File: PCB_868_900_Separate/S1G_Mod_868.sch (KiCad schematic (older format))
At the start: 53 parts, among them J1 S2B-PH-K-S(LF)(SN), Q1 DMG2307L-7, SW1 CUS-12TB, T1 1909763-1, T2 1909763-1, U1 AP7361-33FGE-7, U2 ADF7023BCPZ, X1 ABS07-32.768KHZ-9-T, X2 ABM11-140-26.000MHZ-T3

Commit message: Change and Progress
connecotrs change to SMA, implemented combined PA/LNA match, currently
working on that version as primary. PCB components are placed and board
size is almost set.
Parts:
- removed T1, T2: 1909763-1, PCB_Footprints:1909763-1, symbol 1909763-1
- added T1, T2: 0732511150, PCB_Footprints:0732511150, symbol 0732511150
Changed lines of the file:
@@
 encoding utf-8
 Sheet 1 2
-Title ""
-Date ""
-Rev ""
-Comp ""
-Comment1 ""
+Title "S1G 915MHZ RF RX/TX Module Separate PA/LNA Match"
+Date "2016-11-07"
+Rev "0.1a"
+Comp "GhostPCB"
+Comment1 "Engineered and Drawn By: Adam Vadala-Roth"
 Comment2 ""
 Comment3 ""
@@
 $EndComp
 $Comp
-L 1909763-1 T2
-U 1 1 5817C82C
-P 725 4600
-F 0 "T2" H 700 4825 60  0000 L CNN
-F 1 "1909763-1" H 275 4725 60  0000 L CNN
-F 2 "PCB_Footprints:1909763-1" H 775 4450 60  0001 C CNN
-F 3 "https://media.digikey.com/pdf/PCNs/TE%20Connectivity/E-15-016061(2).pdf" H 425 4775 60  0001 C CNN
-F 4 "0.24000 @ 5000" H 525 4875 60  0001 C CNN "Cost"
-F 5 "8 Sept 2016" H 625 4975 60  0001 C CNN "Date Created"
-F 6 "8 Sept 2016" H 725 5075 60  0001 C CNN "Date Modified"
-F 7 "Adam Vadala-Roth" H 825 5175 60  0001 C CNN "Designer"
-F 8 "1.25mm" H 925 5275 60  0001 C CNN "Height"
-F 9 "Yes" H 1025 5375 60  0001 C CNN "RHoS?"
-F 10 "TE Connectivity AMP Connectors" H 1125 5475 60  0001 C CNN "MFR"
-F 11 "1909763-1" H 1225 5575 60  0001 C CNN "MFR#"
-F 12 "SMT/SMD" H 1325 5675 60  0001 C CNN "Mounting"
-F 13 "2" H 1425 5775 60  0001 C CNN "Pin Count#"
-F 14 "Active" H 1525 5875 60  0001 C CNN "Status"
-F 15 "N/A" H 1625 5975 60  0001 C CNN "Tolerance"
-F 16 "Coaxial RF Connector" H 1725 6075 60  0001 C CNN "Type"
-F 17 "N/A" H 1825 6175 60  0001 C CNN "Voltage"
-F 18 "N/A" H 1925 6275 60  0001 C CNN "Wattage"
-F 19 "50 ohm" H 2025 6375 60  0001 C CNN "Component-Value"
-F 20 "Ultra Miniature Coaxial Connector Jack, Male Pin 50 Ohm Surface Mount Solder" H 2125 6475 60  0001 C CNN "Description"
-	1    725  4600
-	-1   0    0    -1
-$EndComp
-$Comp
 L 0402CS-12NXJL L1
 U 1 1 5817F234
@@
 $EndComp
 $Comp
-L 1909763-1 T1
-U 1 1 5819761C
-P 700 3375
-F 0 "T1" H 675 3600 60  0000 L CNN
-F 1 "1909763-1" H 250 3500 60  0000 L CNN
-F 2 "PCB_Footprints:1909763-1" H 750 3225 60  0001 C CNN
-F 3 "https://media.digikey.com/pdf/PCNs/TE%20Connectivity/E-15-016061(2).pdf" H 400 3550 60  0001 C CNN
-F 4 "0.24000 @ 5000" H 500 3650 60  0001 C CNN "Cost"
-F 5 "8 Sept 2016" H 600 3750 60  0001 C CNN "Date Created"
-F 6 "8 Sept 2016" H 700 3850 60  0001 C CNN "Date Modified"
-F 7 "Adam Vadala-Roth" H 800 3950 60  0001 C CNN "Designer"
-F 8 "1.25mm" H 900 4050 60  0001 C CNN "Height"
-F 9 "Yes" H 1000 4150 60  0001 C CNN "RHoS?"
-F 10 "TE Connectivity AMP Connectors" H 1100 4250 60  0001 C CNN "MFR"
-F 11 "1909763-1" H 1200 4350 60  0001 C CNN "MFR#"
-F 12 "SMT/SMD" H 1300 4450 60  0001 C CNN "Mounting"
-F 13 "2" H 1400 4550 60  0001 C CNN "Pin Count#"
-F 14 "Active" H 1500 4650 60  0001 C CNN "Status"
-F 15 "N/A" H 1600 4750 60  0001 C CNN "Tolerance"
-F 16 "Coaxial RF Connector" H 1700 4850 60  0001 C CNN "Type"
-F 17 "N/A" H 1800 4950 60  0001 C CNN "Voltage"
-F 18 "N/A" H 1900 5050 60  0001 C CNN "Wattage"
-F 19 "50 ohm" H 2000 5150 60  0001 C CNN "Component-Value"
-F 20 "Ultra Miniature Coaxial Connector Jack, Male Pin 50 Ohm Surface Mount Solder" H 2100 5250 60  0001 C CNN "Description"
-	1    700  3375
-	-1   0    0    -1
-$EndComp
-$Comp
 L GND #PWR1
 U 1 1 581979F7
@@
 L S2B-PH-K-S(LF)(SN) J1
 U 1 1 58229495
-P 1050 6125
-F 0 "J1" H 1000 6400 60  0000 C CNN
-F 1 "S2B-PH-K-S(LF)(SN)" H 1450 6325 60  0000 C CNN
-F 2 "PCB_Footprints:S2B-PH-K-S(LF)(SN)" H 900 6200 60  0001 C CNN
-F 3 "http://www.jst-mfg.com/product/pdf/eng/ePH.pdf" H 775 6500 60  0001 C CNN
-F 4 "0.06152 @ 5000" H 875 6600 60  0001 C CNN "Cost"
-F 5 "9 Sept 2016" H 975 6700 60  0001 C CNN "Date Created "
-F 6 "9 Sept 2016" H 1075 6800 60  0001 C CNN "Date Modified"
-F 7 "Adam Vadala-Roth" H 1175 6900 60  0001 C CNN "Designer "
-F 8 "5.5mm" H 1275 7000 60  0001 C CNN "Height"
-F 9 "Yes" H 1375 7100 60  0001 C CNN "RHoS?"
-F 10 "JST Sales America Inc" H 1475 7200 60  0001 C CNN "MFR"
-F 11 "S2B-PH-K-S(LF)(SN)" H 1575 7300 60  0001 C CNN "MFR#"
-F 12 "Through Hole" H 1675 7400 60  0001 C CNN "Mounting"
-F 13 "2" H 1775 7500 60  0001 C CNN "Pin Count#"
-F 14 "Active" H 1875 7600 60  0001 C CNN "Status"
-F 15 "N/A" H 1975 7700 60  0001 C CNN "Tolerance"
-F 16 "Through Hole right angle connector." H 2075 7800 60  0001 C CNN "Type"
-F 17 "N/A" H 2175 7900 60  0001 C CNN "Voltage"
-F 18 "N/A" H 2275 8000 60  0001 C CNN "Wattage"
-F 19 "N/A" H 2375 8100 60  0001 C CNN "Component-Value"
-F 20 "2 Positions Header, Shrouded Connector 0.079\" (2.00mm) Through Hole, Right Angle Tin" H 2475 8200 60  0001 C CNN "Description"
-	1    1050 6125
-	1    0    0    -1
+P 1050 6050
+F 0 "J1" H 1000 6325 60  0000 C CNN
+F 1 "S2B-PH-K-S(LF)(SN)" H 1450 6250 60  0000 C CNN
+F 2 "PCB_Footprints:S2B-PH-K-S(LF)(SN)" H 900 6125 60  0001 C CNN
+F 3 "http://www.jst-mfg.com/product/pdf/eng/ePH.pdf" H 775 6425 60  0001 C CNN
+F 4 "0.06152 @ 5000" H 875 6525 60  0001 C CNN "Cost"
+F 5 "9 Sept 2016" H 975 6625 60  0001 C CNN "Date Created "
+F 6 "9 Sept 2016" H 1075 6725 60  0001 C CNN "Date Modified"
+F 7 "Adam Vadala-Roth" H 1175 6825 60  0001 C CNN "Designer "
+F 8 "5.5mm" H 1275 6925 60  0001 C CNN "Height"
+F 9 "Yes" H 1375 7025 60  0001 C CNN "RHoS?"
+F 10 "JST Sales America Inc" H 1475 7125 60  0001 C CNN "MFR"
+F 11 "S2B-PH-K-S(LF)(SN)" H 1575 7225 60  0001 C CNN "MFR#"
+F 12 "Through Hole" H 1675 7325 60  0001 C CNN "Mounting"
+F 13 "2" H 1775 7425 60  0001 C CNN "Pin Count#"
+F 14 "Active" H 1875 7525 60  0001 C CNN "Status"
+F 15 "N/A" H 1975 7625 60  0001 C CNN "Tolerance"
+F 16 "Through Hole right angle connector." H 2075 7725 60  0001 C CNN "Type"
+F 17 "N/A" H 2175 7825 60  0001 C CNN "Voltage"
+F 18 "N/A" H 2275 7925 60  0001 C CNN "Wattage"
+F 19 "N/A" H 2375 8025 60  0001 C CNN "Component-Value"
+F 20 "2 Positions Header, Shrouded Connector 0.079\" (2.00mm) Through Hole, Right Angle Tin" H 2475 8125 60  0001 C CNN "Description"
+	1    1050 6050
+	1    0    0    1
 $EndComp
 $Comp
@@
 Wire Wire Line
 	9375 3800 8950 3800
+$Comp
+L 0732511150 T1
+U 1 1 5828483C
+P 700 3375
+F 0 "T1" H 700 3575 60  0000 L CNN
+F 1 "0732511150" H 225 3500 60  0000 L CNN
+F 2 "PCB_Footprints:0732511150" H 750 3225 60  0001 C CNN
+F 3 "http://www.molex.com/pdm_docs/sd/732511150_sd.pdf" H 400 3550 60  0001 C CNN
+F 4 "1.929370 @ 1000" H 500 3650 60  0001 C CNN "Cost"
+F 5 "7 Nov 2016" H 600 3750 60  0001 C CNN "Date Created"
+F 6 "7 Nov 2016" H 700 3850 60  0001 C CNN "Date Modified"
+F 7 "Adam Vadala-Roth" H 800 3950 60  0001 C CNN "Designer"
+F 8 "1.25mm" H 900 4050 60  0001 C CNN "Height"
+F 9 "Yes" H 1000 4150 60  0001 C CNN "RHoS?"
+F 10 "Molex, LLC" H 1100 4250 60  0001 C CNN "MFR"
+F 11 "0732511150" H 1200 4350 60  0001 C CNN "MFR#"
+F 12 "SMT/SMD" H 1300 4450 60  0001 C CNN "Mounting"
+F 13 "2" H 1400 4550 60  0001 C CNN "Pin Count#"
+F 14 "Active" H 1500 4650 60  0001 C CNN "Status"
+F 15 "N/A" H 1600 4750 60  0001 C CNN "Tolerance"
+F 16 "SMA Coaxial RF Connector" H 1700 4850 60  0001 C CNN "Type"
+F 17 "N/A" H 1800 4950 60  0001 C CNN "Voltage"
+F 18 "N/A" H 1900 5050 60  0001 C CNN "Wattage"
+F 19 "50 ohm" H 2000 5150 60  0001 C CNN "Component-Value"
+F 20 "SMA Connector Receptacle, Female Socket 50 Ohm Board Edge, End Launch Solder" H 2100 5250 60  0001 C CNN "Description"
+	1    700  3375
+	-1   0    0    -1
+$EndComp
+$Comp
+L 0732511150 T2
+U 1 1 5828637F
+P 725 4600
+F 0 "T2" H 725 4800 60  0000 L CNN
+F 1 "0732511150" H 250 4725 60  0000 L CNN
+F 2 "PCB_Footprints:0732511150" H 775 4450 60  0001 C CNN
+F 3 "http://www.molex.com/pdm_docs/sd/732511150_sd.pdf" H 425 4775 60  0001 C CNN
+F 4 "1.929370 @ 1000" H 525 4875 60  0001 C CNN "Cost"
+F 5 "7 Nov 2016" H 625 4975 60  0001 C CNN "Date Created"
+F 6 "7 Nov 2016" H 725 5075 60  0001 C CNN "Date Modified"
+F 7 "Adam Vadala-Roth" H 825 5175 60  0001 C CNN "Designer"
+F 8 "1.25mm" H 925 5275 60  0001 C CNN "Height"
+F 9 "Yes" H 1025 5375 60  0001 C CNN "RHoS?"
+F 10 "Molex, LLC" H 1125 5475 60  0001 C CNN "MFR"
+F 11 "0732511150" H 1225 5575 60  0001 C CNN "MFR#"
+F 12 "SMT/SMD" H 1325 5675 60  0001 C CNN "Mounting"
+F 13 "2" H 1425 5775 60  0001 C CNN "Pin Count#"
+F 14 "Active" H 1525 5875 60  0001 C CNN "Status"
+F 15 "N/A" H 1625 5975 60  0001 C CNN "Tolerance"
+F 16 "SMA Coaxial RF Connector" H 1725 6075 60  0001 C CNN "Type"
+F 17 "N/A" H 1825 6175 60  0001 C CNN "Voltage"
+F 18 "N/A" H 1925 6275 60  0001 C CNN "Wattage"
+F 19 "50 ohm" H 2025 6375 60  0001 C CNN "Component-Value"
+F 20 "SMA Connector Receptacle, Female Socket 50 Ohm Board Edge, End Launch Solder" H 2125 6475 60  0001 C CNN "Description"
+	1    725  4600
+	-1   0    0    -1
+$EndComp
 $EndSCHEMATC

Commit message: License added and dedicated PA/LNA Match
Working on the separate PA/LNA match version. also added cern license
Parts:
- removed J1: S2B-PH-K-S(LF)(SN), PCB_Footprints:S2B-PH-K-S(LF)(SN), symbol S2B-PH-K-S(LF)(SN)
- added SH1: 36103205, PCB_Footprints:36103205, symbol 36103205
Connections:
- wire segments 89 -> 90
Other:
- note added: "S1G-RF 915MHZ Sub 1GHZ RF Radio Separate PA & LNA Match"
- note removed: "S1G-Mod 915MHZ Sub 1GHZ RF RX/TX Module"
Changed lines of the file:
@@
 $EndComp
 $Comp
-L GND #PWR4
+L GND #PWR3
 U 1 1 58174222
 P 2000 5050
-F 0 "#PWR4" H 2000 4800 50  0001 C CNN
+F 0 "#PWR3" H 2000 4800 50  0001 C CNN
 F 1 "GND" H 2005 4877 50  0000 C CNN
 F 2 "" H 2000 5050 50  0000 C CNN
@@
 $EndComp
 $Comp
-L GND #PWR6
+L GND #PWR5
 U 1 1 581744A7
 P 2800 5050
-F 0 "#PWR6" H 2800 4800 50  0001 C CNN
+F 0 "#PWR5" H 2800 4800 50  0001 C CNN
 F 1 "GND" H 2805 4877 50  0000 C CNN
 F 2 "" H 2800 5050 50  0000 C CNN
@@
 $EndComp
 $Comp
-L GND #PWR11
+L GND #PWR10
 U 1 1 5816BC64
 P 4000 6500
-F 0 "#PWR11" H 4000 6250 50  0001 C CNN
+F 0 "#PWR10" H 4000 6250 50  0001 C CNN
 F 1 "GND" H 4005 6327 50  0000 C CNN
 F 2 "" H 4000 6500 50  0000 C CNN
@@
 $EndComp
 $Comp
-L GND #PWR9
+L GND #PWR8
 U 1 1 5817CEBD
 P 3650 2200
-F 0 "#PWR9" H 3650 1950 50  0001 C CNN
+F 0 "#PWR8" H 3650 1950 50  0001 C CNN
 F 1 "GND" H 3655 2027 50  0000 C CNN
 F 2 "" H 3650 2200 50  0000 C CNN
@@
 $EndComp
 $Comp
-L +3.3V #PWR7
+L +3.3V #PWR6
 U 1 1 5817CF98
 P 3150 1750
-F 0 "#PWR7" H 3150 1600 50  0001 C CNN
+F 0 "#PWR6" H 3150 1600 50  0001 C CNN
 F 1 "+3.3V" H 3165 1923 50  0000 C CNN
 F 2 "" H 3150 1750 50  0000 C CNN
@@
 $EndComp
 $Comp
-L GND #PWR8
+L GND #PWR7
 U 1 1 5818E84F
 P 3600 5050
-F 0 "#PWR8" H 3600 4800 50  0001 C CNN
+F 0 "#PWR7" H 3600 4800 50  0001 C CNN
 F 1 "GND" H 3605 4877 50  0000 C CNN
 F 2 "" H 3600 5050 50  0000 C CNN
@@
 $EndComp
 $Comp
-L GND #PWR10
+L GND #PWR9
 U 1 1 58195E9E
 P 3675 4100
-F 0 "#PWR10" H 3675 3850 50  0001 C CNN
+F 0 "#PWR9" H 3675 3850 50  0001 C CNN
 F 1 "GND" H 3680 3927 50  0000 C CNN
 F 2 "" H 3675 4100 50  0000 C CNN
@@
 $EndComp
 $Comp
-L GND #PWR5
+L GND #PWR4
 U 1 1 58196935
 P 2800 3025
-F 0 "#PWR5" H 2800 2775 50  0001 C CNN
+F 0 "#PWR4" H 2800 2775 50  0001 C CNN
 F 1 "GND" H 2805 2852 50  0000 C CNN
 F 2 "" H 2800 3025 50  0000 C CNN
@@
 	1    0    0    -1
 $EndComp
-Text Notes 2575 975  0    197  ~ 39
-S1G-Mod 915MHZ Sub 1GHZ RF RX/TX Module
+Text Notes 1075 975  0    197  ~ 39
+S1G-RF  915MHZ Sub 1GHZ RF Radio Separate PA & LNA Match
 $Comp
 L RC1005F103CS R3
@@
 F7 "SYNC" I L 9375 3700 60
 F8 "VBUS" I L 9375 3800 60
+F9 "VIN" I L 9375 3900 60
 $EndSheet
 $Comp
@@
 $EndComp
 $Comp
-L S2B-PH-K-S(LF)(SN) J1
-U 1 1 58229495
-P 1050 6050
-F 0 "J1" H 1000 6325 60  0000 C CNN
-F 1 "S2B-PH-K-S(LF)(SN)" H 1450 6250 60  0000 C CNN
-F 2 "PCB_Footprints:S2B-PH-K-S(LF)(SN)" H 900 6125 60  0001 C CNN
-F 3 "http://www.jst-mfg.com/product/pdf/eng/ePH.pdf" H 775 6425 60  0001 C CNN
-F 4 "0.06152 @ 5000" H 875 6525 60  0001 C CNN "Cost"
-F 5 "9 Sept 2016" H 975 6625 60  0001 C CNN "Date Created "
-F 6 "9 Sept 2016" H 1075 6725 60  0001 C CNN "Date Modified"
-F 7 "Adam Vadala-Roth" H 1175 6825 60  0001 C CNN "Designer "
-F 8 "5.5mm" H 1275 6925 60  0001 C CNN "Height"
-F 9 "Yes" H 1375 7025 60  0001 C CNN "RHoS?"
-F 10 "JST Sales America Inc" H 1475 7125 60  0001 C CNN "MFR"
-F 11 "S2B-PH-K-S(LF)(SN)" H 1575 7225 60  0001 C CNN "MFR#"
-F 12 "Through Hole" H 1675 7325 60  0001 C CNN "Mounting"
-F 13 "2" H 1775 7425 60  0001 C CNN "Pin Count#"
-F 14 "Active" H 1875 7525 60  0001 C CNN "Status"
-F 15 "N/A" H 1975 7625 60  0001 C CNN "Tolerance"
-F 16 "Through Hole right angle connector." H 2075 7725 60  0001 C CNN "Type"
-F 17 "N/A" H 2175 7825 60  0001 C CNN "Voltage"
-F 18 "N/A" H 2275 7925 60  0001 C CNN "Wattage"
-F 19 "N/A" H 2375 8025 60  0001 C CNN "Component-Value"
-F 20 "2 Positions Header, Shrouded Connector 0.079\" (2.00mm) Through Hole, Right Angle Tin" H 2475 8125 60  0001 C CNN "Description"
-	1    1050 6050
-	1    0    0    1
-$EndComp
-$Comp
 L M2.5_Hole H1
 U 1 1 58229636
@@
 Wire Wire Line
 	2225 6050 1250 6050
-$Comp
-L GND #PWR3
-U 1 1 582360D6
-P 1250 6125
-F 0 "#PWR3" H 1250 5875 50  0001 C CNN
-F 1 "GND" H 1255 5952 50  0000 C CNN
-F 2 "" H 1250 6125 50  0000 C CNN
-F 3 "" H 1250 6125 50  0000 C CNN
-	1    1250 6125
-	1    0    0    -1
-$EndComp
 Text Label 1250 6050 0    60   ~ 0
 PSU_IN
@@
 	-1   0    0    -1
 $EndComp
+Text Label 9025 3900 0    60   ~ 0
+PSU_IN
+Wire Wire Line
+	9375 3900 8950 3900
+$Comp
+L 36103205 SH1
+U 1 1 5825B3C7
+P 4900 5250
+F 0 "SH1" H 4818 5587 60  0000 C CNN
+F 1 "36103205" H 4818 5481 60  0000 C CNN
+F 2 "PCB_Footprints:36103205" H 4250 5800 60  0001 C CNN
+F 3 "http://katalog.we-online.de/pbs/datasheet/36103205.pdf" H 4250 5900 60  0001 C CNN
+F 4 "3.49000" H 4850 6000 60  0001 C CNN "Cost"
+F 5 "9 Nov 2016" H 5050 6200 60  0001 C CNN "Date Created"
+F 6 "9 Nov 2016" H 5050 6200 60  0001 C CNN "Date Modified"
+F 7 "Adam Vadala-Roth" H 5150 6300 60  0001 C CNN "Designer"
+F 8 "2.5mm" H 5250 6400 60  0001 C CNN "Height"
+F 9 "Yes" H 5350 6500 60  0001 C CNN "RHoS?"
+F 10 "Wurth Electronics Inc" H 5450 6600 60  0001 C CNN "MFR"
+F 11 "36103205" H 5550 6700 60  0001 C CNN "MFR#"
+F 12 "SMT/SMD" H 5650 6800 60  0001 C CNN "Mounting"
+F 13 "None" H 5750 6900 60  0001 C CNN "Pin Count#"
+F 14 "Active" H 5850 7000 60  0001 C CNN "Status"
+F 15 "N/A" H 5950 7100 60  0001 C CNN "Tolerance"
+F 16 "RF Shield" H 6050 7200 60  0001 C CNN "Type"
+F 17 "N/A" H 6150 7300 60  0001 C CNN "Voltage"
+F 18 "N/A" H 6250 7400 60  0001 C CNN "Wattage"
+F 19 "N/A" H 6350 7500 60  0001 C CNN "Component-Value"
+F 20 "RF Shield Frame 0.827\" (21.00mm) X 0.827\" (21.00mm) Surface Mount" H 6450 7600 60  0001 C CNN "Description"
+	1    4900 5250
+	1    0    0    -1
+$EndComp
+$Comp
+L GND #PWR11
+U 1 1 5825B89E
+P 4150 5250
+F 0 "#PWR11" H 4150 5000 50  0001 C CNN
+F 1 "GND" H 4155 5077 50  0000 C CNN
+F 2 "" H 4150 5250 50  0000 C CNN
+F 3 "" H 4150 5250 50  0000 C CNN
+	1    4150 5250
+	1    0    0    -1
+$EndComp
 $EndSCHEMATC

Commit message: PCBs Tweaked A lot
PCBs have been tweaked. The separate implementation has been finished
but also has GPIOs from the MCU broken out to the connector, same for
the combined implementation. Both boards now have power indication LEDs
(red).
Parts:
- removed R4: RC1608J202CS, PCB_Footprints:R0603, symbol RC1608J202CS
- added LED4: LTST-C193KRKT-5A, PCB_Footprints:LED0603, symbol LTST-C193KRKT-5A
- added R10, R4: RC1005F102CS, PCB_Footprints:R0402, symbol RC1005F102CS
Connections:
- wire segments 90 -> 91

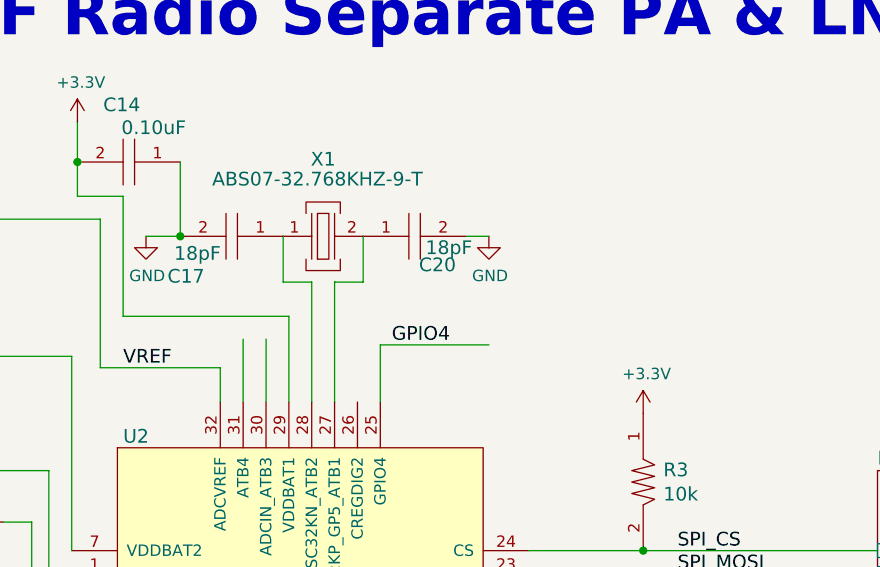
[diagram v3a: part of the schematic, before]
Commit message: Grounding and Adapter
Grounding changed on both versions of the 915MHZ/868MHZ versions of the
radio both the combined and separate antenna versions. Also an adapter
is being developed for alternative connection options.
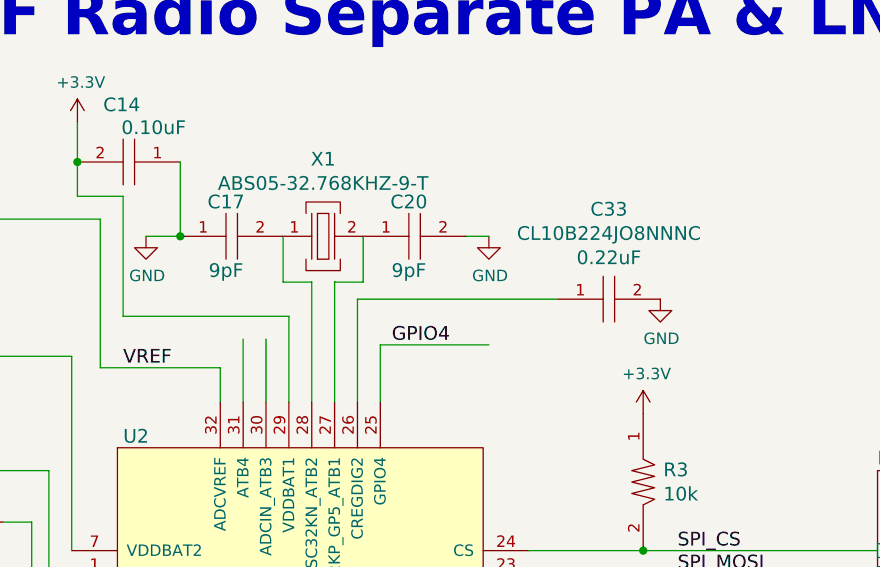
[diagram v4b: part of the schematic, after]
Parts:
- removed C17, C20: CL05C180GB5NCNC, PCB_Footprints:C0402, symbol CL05C180GB5NCNC
- removed X1: ABS07-32.768KHZ-9-T, PCB_Footprints:ABS07-32.768KHZ-9-T, symbol ABS07-32.768KHZ-9-T
- added C17, C20: CL05C090CB5NNNC, PCB_Footprints:C0402, symbol CL05C090CB5NNNC
- added C33: CL10B224JO8NNNC, PCB_Footprints:C0402, symbol CL10B224JO8NNNC
- added X1: ABS05-32.768KHZ-9-T, PCB_Footprints:ABS05-32.768KHZ-9-T, symbol ABS05-32.768KHZ-9-T
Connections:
- wire segments 91 -> 93
